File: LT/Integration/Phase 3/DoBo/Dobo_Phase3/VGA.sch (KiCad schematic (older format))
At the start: 20 parts, among them J11 Conn_01x02_Male, J13 Conn_Coaxial, U3 LMH6624, U4 LMH6505

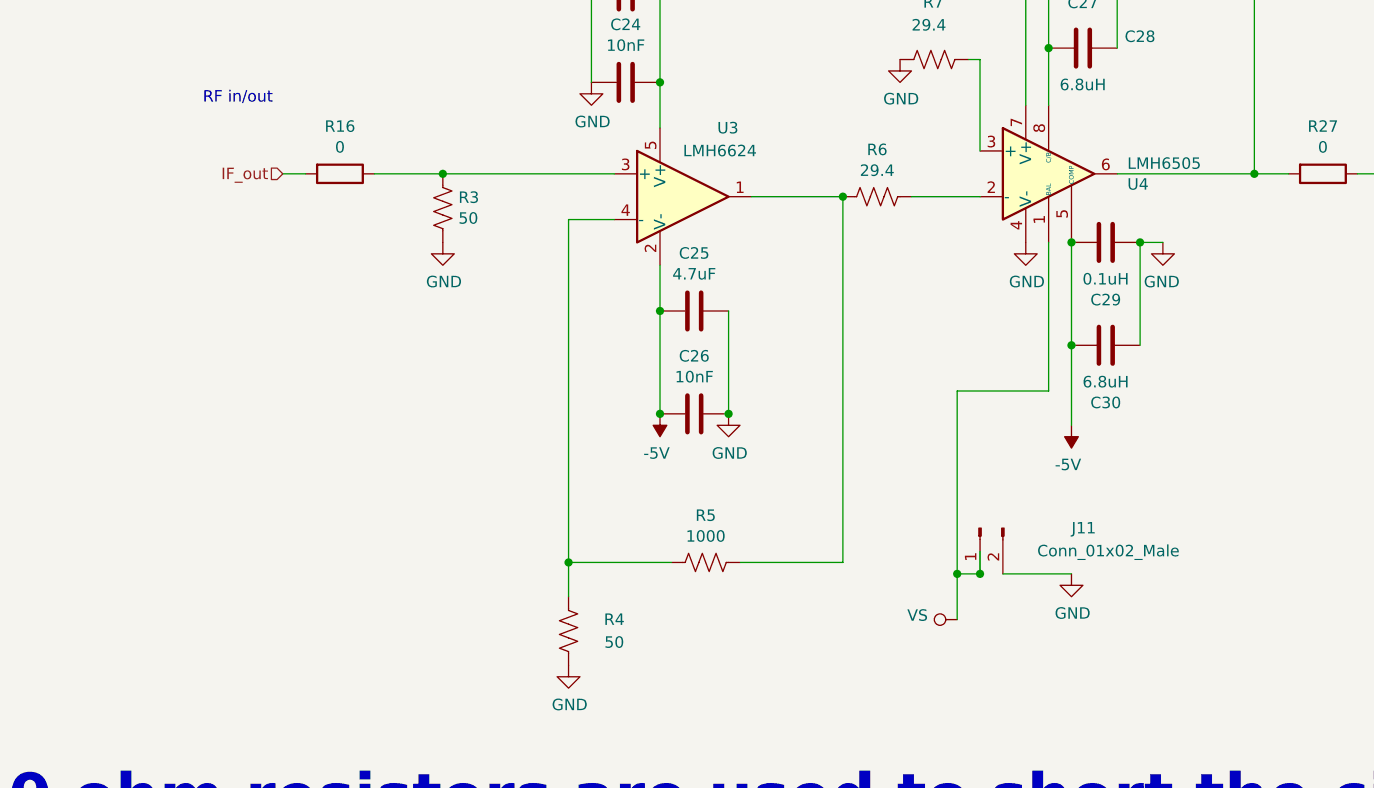
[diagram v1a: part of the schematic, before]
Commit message: Added the completed layout for the DoBo Phase 3
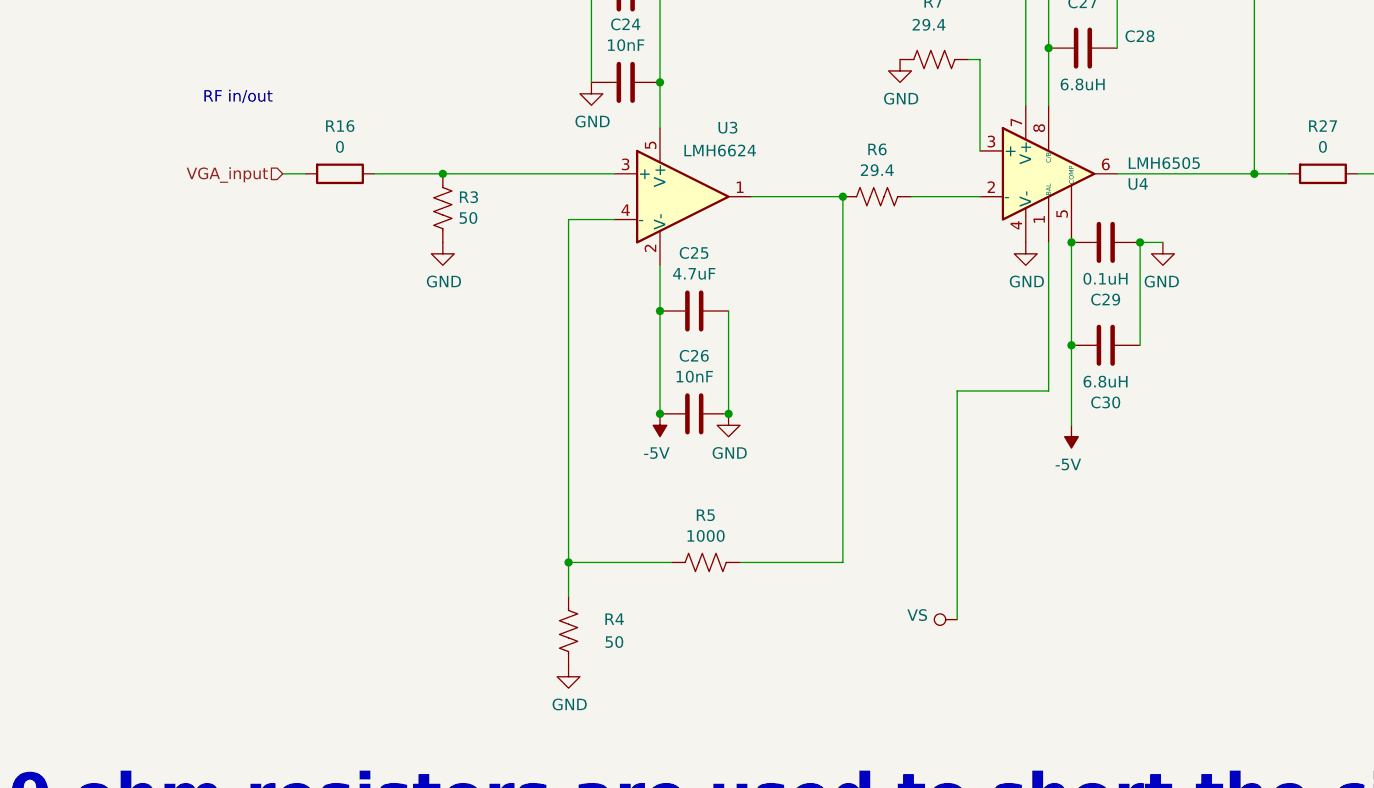
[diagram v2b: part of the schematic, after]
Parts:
- removed J11: Conn_01x02_Male, Connector_PinHeader_2.54mm:PinHeader_1x02_P2.54mm_Vertical, symbol Connector:Conn_01x02_Male
- J13: footprint Connector_Coaxial:SMA_Amphenol_132289_EdgeMount -> Connector_Coaxial:SMA_Amphenol_132291_Vertical
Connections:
- net IF_out renamed VGA_input
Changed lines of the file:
@@
 $Descr A4 11693 8268
 encoding utf-8
-Sheet 5 10
+Sheet 4 10
 Title ""
 Date ""
@@
 Connection ~ 5800 3050
 $Comp
-L Connector:Conn_01x02_Male J11
-U 1 1 5E50257A
-P 5100 4300
-F 0 "J11" V 5100 3900 50  0000 R CNN
-F 1 "Conn_01x02_Male" V 5200 4050 50  0000 R CNN
-F 2 "Connector_PinHeader_2.54mm:PinHeader_1x02_P2.54mm_Vertical" H 5100 4300 50  0001 C CNN
-F 3 "~" H 5100 4300 50  0001 C CNN
-	1    5100 4300
-	0    -1   1    0
-$EndComp
-Wire Wire Line
-	5100 4400 5100 4500
-Wire Wire Line
-	5000 4500 5100 4500
-Connection ~ 5100 4500
-$Comp
 L Device:C C27
 U 1 1 5E509049
@@
 $EndComp
 $Comp
-L power:GND #PWR033
-U 1 1 5E52AA4B
-P 5500 4500
-F 0 "#PWR033" H 5500 4250 50  0001 C CNN
-F 1 "GND" H 5505 4327 50  0000 C CNN
-F 2 "" H 5500 4500 50  0001 C CNN
-F 3 "" H 5500 4500 50  0001 C CNN
-	1    5500 4500
-	1    0    0    -1
-$EndComp
-$Comp
 L power:VS #PWR029
 U 1 1 5E52D788
@@
 $EndComp
 Wire Wire Line
-	5000 4700 5000 4500
-Wire Wire Line
 	5100 2650 5100 2250
 Wire Wire Line
@@
 F 0 "J13" H 7300 2725 50  0000 L CNN
 F 1 "Conn_Coaxial" H 7300 2634 50  0000 L CNN
-F 2 "Connector_Coaxial:SMA_Amphenol_132289_EdgeMount" H 7200 2750 50  0001 C CNN
+F 2 "Connector_Coaxial:SMA_Amphenol_132291_Vertical" H 7200 2750 50  0001 C CNN
 F 3 " ~" H 7200 2750 50  0001 C CNN
 	1    7200 2750
@@
 Wire Wire Line
 	5400 3700 5000 3700
-Wire Wire Line
-	5000 3700 5000 4500
-Connection ~ 5000 4500
-Wire Wire Line
-	5200 4500 5500 4500
 Text HLabel 2050 2750 0    50   Input ~ 0
-IF_out
+VGA_input
 Wire Wire Line
 	2050 2750 2150 2750
@@
 	1    0    0    -1
 $EndComp
+Wire Wire Line
+	5000 3700 5000 4700
 $EndSCHEMATC

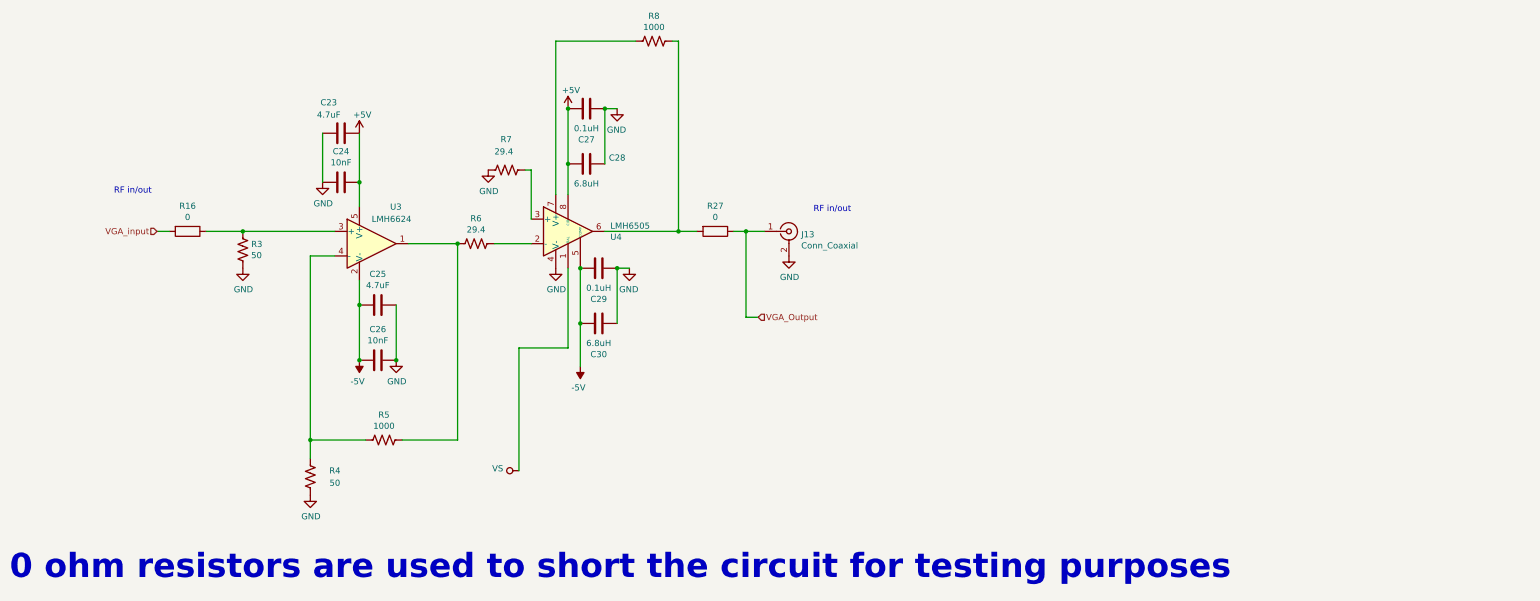
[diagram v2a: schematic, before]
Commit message: Adding the DoBo Phase 3 integration with all traces routed
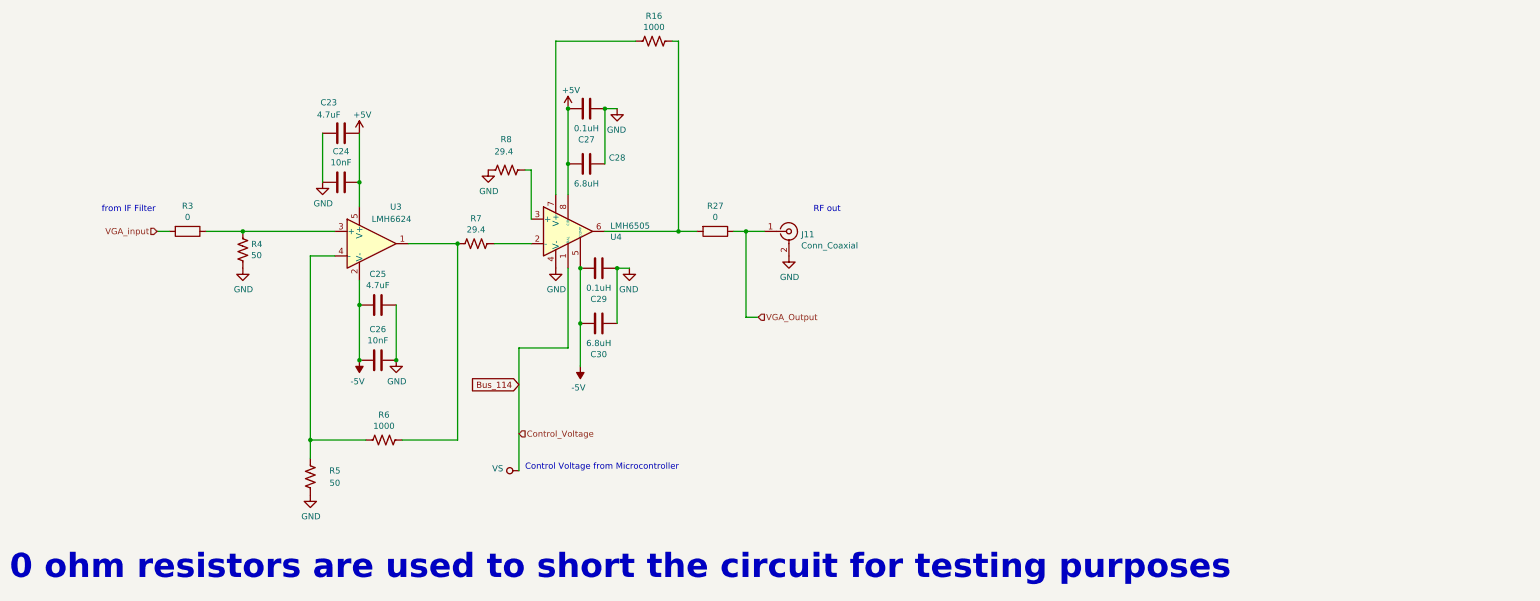
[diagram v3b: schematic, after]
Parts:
- renumbered J13 to J11, R8 to R16, R16 to R3, R3 to R4, R4 to R5, R5 to R6, R6 to R7, R7 to R8
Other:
- note added: "Control Voltage from Microcontroller"
- note added: "RF out"
- note added: "from IF Filter"
- note removed: "RF in/out"
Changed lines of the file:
@@
 $Descr A4 11693 8268
 encoding utf-8
-Sheet 4 10
+Sheet 10 10
 Title ""
 Date ""
@@
 $EndComp
 $Comp
-L Device:R_US R3
+L Device:R_US R4
 U 1 1 5E4E76AD
 P 2750 2900
-F 0 "R3" H 2682 2854 50  0000 R CNN
+F 0 "R4" H 2682 2854 50  0000 R CNN
 F 1 "50" H 2682 2945 50  0000 R CNN
 F 2 "Resistor_SMD:R_0402_1005Metric" V 2790 2890 50  0001 C CNN
@@
 Connection ~ 2750 2750
 $Comp
-L power:GND #PWR021
+L power:GND #PWR0114
 U 1 1 5E4EEC87
 P 2750 3050
-F 0 "#PWR021" H 2750 2800 50  0001 C CNN
+F 0 "#PWR0114" H 2750 2800 50  0001 C CNN
 F 1 "GND" H 2755 2877 50  0000 C CNN
 F 2 "" H 2750 3050 50  0001 C CNN
@@
 	1    0    0    -1
 $EndComp
-Text Notes 1700 2450 0    50   ~ 0
-RF in/out
+Text Notes 1600 2600 0    50   ~ 0
+from IF Filter
 Wire Wire Line
 	3700 3150 3700 3350
@@
 	3700 3350 3700 3800
 $Comp
-L power:GND #PWR027
+L power:GND #PWR0120
 U 1 1 5E4F2257
 P 4000 3800
-F 0 "#PWR027" H 4000 3550 50  0001 C CNN
+F 0 "#PWR0120" H 4000 3550 50  0001 C CNN
 F 1 "GND" H 4005 3627 50  0000 C CNN
 F 2 "" H 4000 3800 50  0001 C CNN
@@
 Connection ~ 4000 3800
 $Comp
-L power:-5V #PWR025
+L power:-5V #PWR0162
 U 1 1 5E4F25CA
 P 3700 3800
-F 0 "#PWR025" H 3700 3900 50  0001 C CNN
+F 0 "#PWR0162" H 3700 3900 50  0001 C CNN
 F 1 "-5V" H 3715 3973 50  0000 C CNN
 F 2 "" H 3700 3800 50  0001 C CNN
@@
 	3400 1950 3400 2350
 $Comp
-L power:GND #PWR023
+L power:GND #PWR0163
 U 1 1 5E4F35D0
 P 3400 2350
-F 0 "#PWR023" H 3400 2100 50  0001 C CNN
+F 0 "#PWR0163" H 3400 2100 50  0001 C CNN
 F 1 "GND" H 3405 2177 50  0000 C CNN
 F 2 "" H 3400 2350 50  0001 C CNN
@@
 	4500 2850 4100 2850
 $Comp
-L Device:R_US R5
+L Device:R_US R6
 U 1 1 5E4F7D30
 P 3900 4450
-F 0 "R5" V 3695 4450 50  0000 C CNN
+F 0 "R6" V 3695 4450 50  0000 C CNN
 F 1 "1000" V 3786 4450 50  0000 C CNN
 F 2 "Resistor_SMD:R_0402_1005Metric" V 3940 4440 50  0001 C CNN
@@
 	4050 4450 4500 4450
 $Comp
-L Device:R_US R4
+L Device:R_US R5
 U 1 1 5E4F8F93
 P 3300 4750
-F 0 "R4" H 3500 4800 50  0000 C CNN
+F 0 "R5" H 3500 4800 50  0000 C CNN
 F 1 "50" H 3500 4700 50  0000 C CNN
 F 2 "Resistor_SMD:R_0402_1005Metric" V 3340 4740 50  0001 C CNN
@@
 $EndComp
 $Comp
-L power:GND #PWR022
+L power:GND #PWR0164
 U 1 1 5E4FA288
 P 3300 4900
-F 0 "#PWR022" H 3300 4650 50  0001 C CNN
+F 0 "#PWR0164" H 3300 4650 50  0001 C CNN
 F 1 "GND" H 3305 4727 50  0000 C CNN
 F 2 "" H 3300 4900 50  0001 C CNN
@@
 Connection ~ 3300 4450
 $Comp
-L Device:R_US R6
+L Device:R_US R7
 U 1 1 5E4FB3D6
 P 4650 2850
-F 0 "R6" V 4445 2850 50  0000 C CNN
+F 0 "R7" V 4445 2850 50  0000 C CNN
 F 1 "29.4" V 4536 2850 50  0000 C CNN
 F 2 "Resistor_SMD:R_0402_1005Metric" V 4690 2840 50  0001 C CNN
@@
 	4800 2850 5100 2850
 $Comp
-L Device:R_US R7
+L Device:R_US R8
 U 1 1 5E4FC089
 P 4900 2250
-F 0 "R7" V 4650 2200 50  0000 L CNN
+F 0 "R8" V 4650 2200 50  0000 L CNN
 F 1 "29.4" V 4750 2150 50  0000 L CNN
 F 2 "Resistor_SMD:R_0402_1005Metric" V 4940 2240 50  0001 C CNN
@@
 $EndComp
 $Comp
-L power:GND #PWR028
+L power:GND #PWR0165
 U 1 1 5E4FD2C3
 P 4750 2250
-F 0 "#PWR028" H 4750 2000 50  0001 C CNN
+F 0 "#PWR0165" H 4750 2000 50  0001 C CNN
 F 1 "GND" H 4755 2077 50  0000 C CNN
 F 2 "" H 4750 2250 50  0001 C CNN
@@
 	5800 3500 5800 3050
 $Comp
-L power:GND #PWR035
+L power:GND #PWR0166
 U 1 1 5E4FF9FC
 P 5900 3050
-F 0 "#PWR035" H 5900 2800 50  0001 C CNN
+F 0 "#PWR0166" H 5900 2800 50  0001 C CNN
 F 1 "GND" H 5905 2877 50  0000 C CNN
 F 2 "" H 5900 3050 50  0001 C CNN
@@
 	5700 2200 5700 1750
 $Comp
-L power:GND #PWR034
+L power:GND #PWR0167
 U 1 1 5E509059
 P 5800 1750
-F 0 "#PWR034" H 5800 1500 50  0001 C CNN
+F 0 "#PWR0167" H 5800 1500 50  0001 C CNN
 F 1 "GND" H 5805 1577 50  0000 C CNN
 F 2 "" H 5800 1750 50  0001 C CNN
@@
 	5700 1750 5800 1750
 $Comp
-L power:GND #PWR030
+L power:GND #PWR0168
 U 1 1 5E510956
 P 5300 3050
-F 0 "#PWR030" H 5300 2800 50  0001 C CNN
+F 0 "#PWR0168" H 5300 2800 50  0001 C CNN
 F 1 "GND" H 5305 2877 50  0000 C CNN
 F 2 "" H 5300 3050 50  0001 C CNN
@@
 Connection ~ 5500 3500
 $Comp
-L power:+5V #PWR031
+L power:+5V #PWR0169
 U 1 1 5E5241D2
 P 5400 1750
-F 0 "#PWR031" H 5400 1600 50  0001 C CNN
+F 0 "#PWR0169" H 5400 1600 50  0001 C CNN
 F 1 "+5V" H 5350 1900 50  0000 L CNN
 F 2 "" H 5400 1750 50  0001 C CNN
@@
 $EndComp
 $Comp
-L power:VS #PWR029
+L power:VS #PWR0170
 U 1 1 5E52D788
 P 5000 4700
-F 0 "#PWR029" H 4800 4550 50  0001 C CNN
+F 0 "#PWR0170" H 4800 4550 50  0001 C CNN
 F 1 "VS" V 5018 4828 50  0000 L CNN
 F 2 "" H 5000 4700 50  0001 C CNN
@@
 	5400 1750 5400 2200
 Text Notes 7400 2600 0    50   ~ 0
-RF in/out
-$Comp
-L power:GND #PWR036
+RF out
+$Comp
+L power:GND #PWR0171
 U 1 1 5E53591C
 P 7200 2950
-F 0 "#PWR036" H 7200 2700 50  0001 C CNN
+F 0 "#PWR0171" H 7200 2700 50  0001 C CNN
 F 1 "GND" H 7205 2777 50  0000 C CNN
 F 2 "" H 7200 2950 50  0001 C CNN
@@
 $EndComp
 $Comp
-L Connector:Conn_Coaxial J13
+L Connector:Conn_Coaxial J11
 U 1 1 5E532DA5
 P 7200 2750
-F 0 "J13" H 7300 2725 50  0000 L CNN
+F 0 "J11" H 7300 2725 50  0000 L CNN
 F 1 "Conn_Coaxial" H 7300 2634 50  0000 L CNN
 F 2 "Connector_Coaxial:SMA_Amphenol_132291_Vertical" H 7200 2750 50  0001 C CNN
@@
 	5400 2450 5400 2200
 $Comp
-L Device:R_US R8
+L Device:R_US R16
 U 1 1 5E531598
 P 6100 1200
-F 0 "R8" V 5895 1200 50  0000 C CNN
+F 0 "R16" V 5895 1200 50  0000 C CNN
 F 1 "1000" V 5986 1200 50  0000 C CNN
 F 2 "Resistor_SMD:R_0402_1005Metric" V 6140 1190 50  0001 C CNN
@@
 	2050 2750 2150 2750
 $Comp
-L Device:R R16
+L Device:R R3
 U 1 1 5EB7CD15
 P 2300 2750
-F 0 "R16" V 2093 2750 50  0000 C CNN
+F 0 "R3" V 2093 2750 50  0000 C CNN
 F 1 "0" V 2184 2750 50  0000 C CNN
 F 2 "Resistor_SMD:R_0805_2012Metric_Pad1.15x1.40mm_HandSolder" V 2230 2750 50  0001 C CNN
@@
 	6850 2750 7000 2750
 $Comp
-L power:-5V #PWR0114
+L power:-5V #PWR0172
 U 1 1 5EE455DE
 P 5500 3850
-F 0 "#PWR0114" H 5500 3950 50  0001 C CNN
+F 0 "#PWR0172" H 5500 3950 50  0001 C CNN
 F 1 "-5V" H 5515 4023 50  0000 C CNN
 F 2 "" H 5500 3850 50  0001 C CNN
@@
 $EndComp
 $Comp
-L power:+5V #PWR0120
+L power:+5V #PWR0173
 U 1 1 5EE46AEE
 P 3700 1950
-F 0 "#PWR0120" H 3700 1800 50  0001 C CNN
+F 0 "#PWR0173" H 3700 1800 50  0001 C CNN
 F 1 "+5V" H 3650 2100 50  0000 L CNN
 F 2 "" H 3700 1950 50  0001 C CNN
@@
 Wire Wire Line
 	5000 3700 5000 4700
+Text HLabel 5000 4400 2    50   Input ~ 0
+Control_Voltage
+Text Notes 5050 4700 0    50   ~ 0
+Control Voltage from Microcontroller
+Text GLabel 5000 4000 0    50   Input ~ 0
+Bus_114
 $EndSCHEMATC

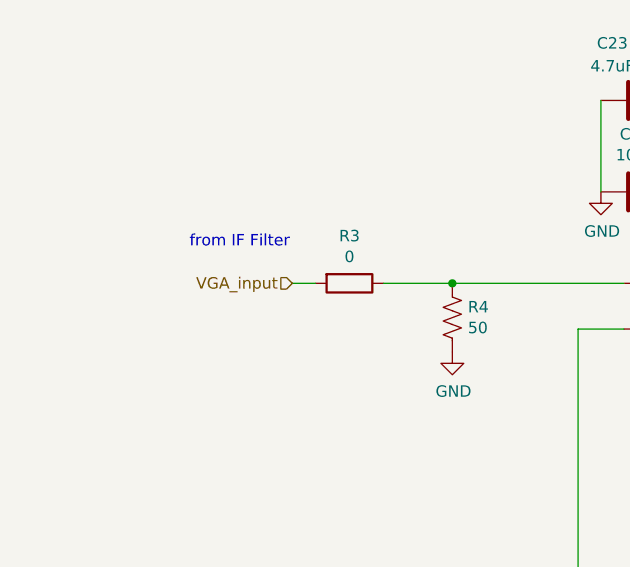
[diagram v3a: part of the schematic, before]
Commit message: Added the finalized layouts for the Mobo and Dobo Phase 3, as well as the preliminary layout for Phase 4 of both boards
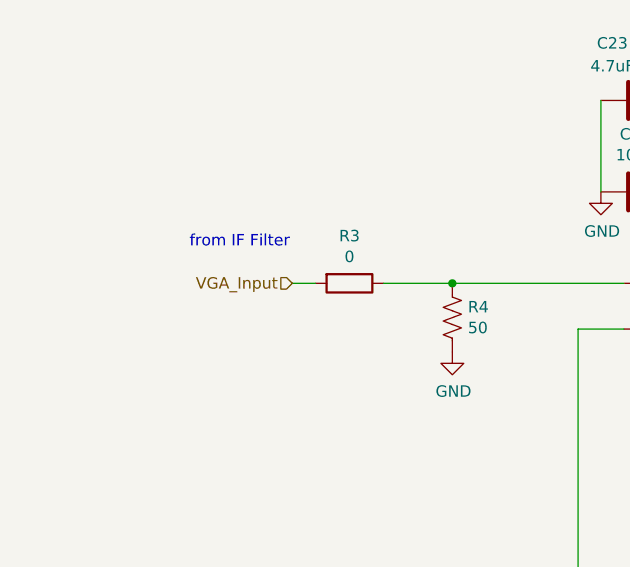
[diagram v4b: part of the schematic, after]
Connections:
- net VGA_input renamed VGA_Input
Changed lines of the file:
@@
 $Descr A4 11693 8268
 encoding utf-8
-Sheet 10 10
+Sheet 9 10
 Title ""
 Date ""
@@
 	5400 3700 5000 3700
 Text HLabel 2050 2750 0    50   Input ~ 0
-VGA_input
+VGA_Input
 Wire Wire Line
 	2050 2750 2150 2750
